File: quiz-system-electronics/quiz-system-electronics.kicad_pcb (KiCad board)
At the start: 2 copper layers, 25 parts, among them U1 74HC595, U2 74HC595, U3 74HC595, U4 ULN2803A, U5 ULN2803A

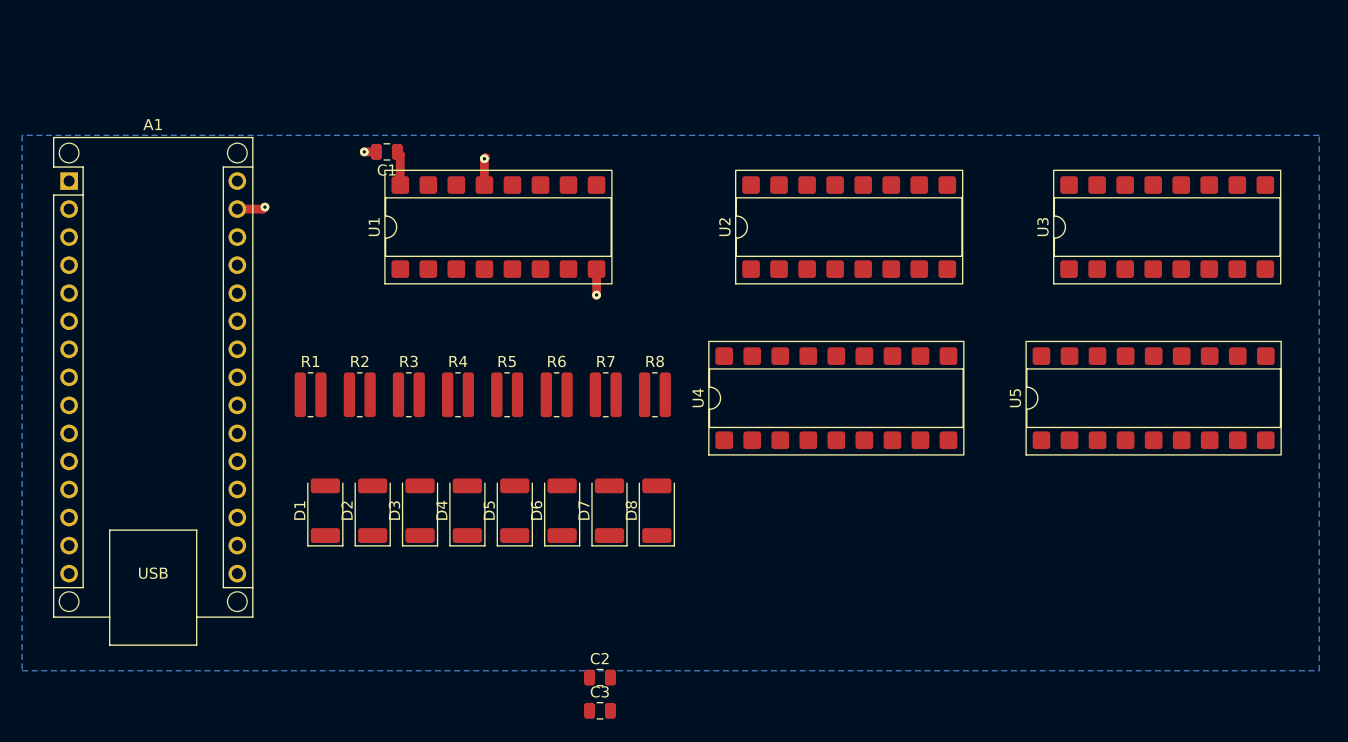
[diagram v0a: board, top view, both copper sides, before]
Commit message: Updated schematic and started to connect PCB
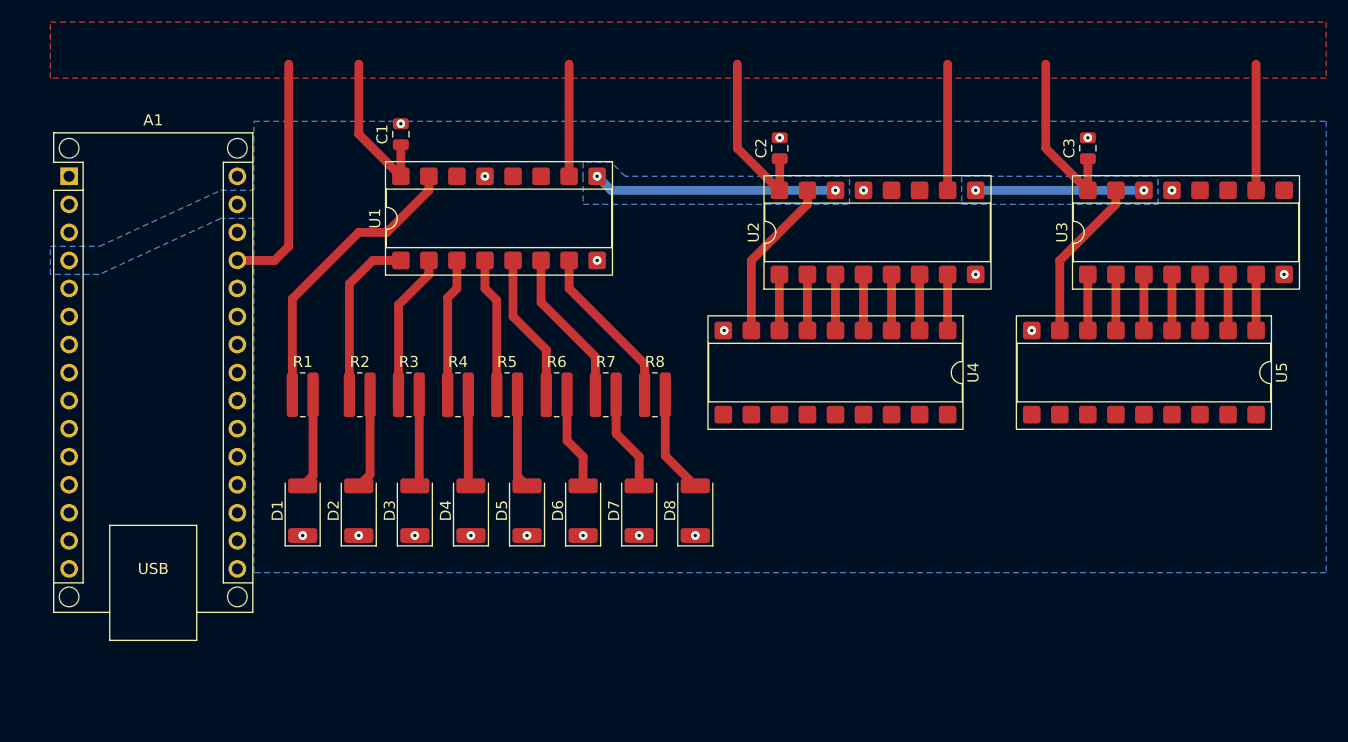
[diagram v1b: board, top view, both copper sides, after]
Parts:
- moved C3 67.5 mm to (129.5, 26.7), turned to 90 degrees
- moved C2 50.6 mm to (101.6, 26.7), turned to 90 degrees
- moved D8 3.48 mm to (94.0, 59.5)
- moved D7 2.69 mm to (88.9, 59.5)
- moved U2 2.61 mm to (110.5, 34.3)
- moved U5 2.48 mm to (134.6, 47.0), turned to -90 degrees
- moved U4 2.32 mm to (106.7, 47.0), turned to -90 degrees
- moved D1 2.05 mm to (58.4, 59.5)
- moved C1 2.04 mm to (67.3, 25.4), turned to 90 degrees
- moved D6 1.90 mm to (83.8, 59.5)
- moved U3 1.77 mm to (138.4, 34.3)
- moved D2 1.26 mm to (63.5, 59.5)
- moved D5 1.11 mm to (78.7, 59.5)
- moved U1 0.79 mm to (76.2, 33.0)
- moved R1 0.72 mm to (58.4, 49.0)
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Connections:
- U4 pad 1: Net-(U2-QA) -> Net-(U2-QH)
- U4 pad 2: Net-(U2-QB) -> Net-(U2-QG)
- U4 pad 3: Net-(U2-QC) -> Net-(U2-QF)
- U4 pad 4: Net-(U2-QD) -> Net-(U2-QE)
- U4 pad 5: Net-(U2-QE) -> Net-(U2-QD)
- U4 pad 6: Net-(U2-QF) -> Net-(U2-QC)
- U4 pad 7: Net-(U2-QG) -> Net-(U2-QB)
- U4 pad 8: Net-(U2-QH) -> Net-(U2-QA)
- U5 pad 1: Net-(U3-QA) -> Net-(U3-QH)
- U5 pad 2: Net-(U3-QB) -> Net-(U3-QG)
- U5 pad 3: Net-(U3-QC) -> Net-(U3-QF)
- U5 pad 4: Net-(U3-QD) -> Net-(U3-QE)
- U5 pad 5: Net-(U3-QE) -> Net-(U3-QD)
- U5 pad 6: Net-(U3-QF) -> Net-(U3-QC)
- U5 pad 7: Net-(U3-QG) -> Net-(U3-QB)
- U5 pad 8: Net-(U3-QH) -> Net-(U3-QA)
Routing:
- net +5V: track 3.11 -> 101.1 mm
- net Net-(U1-QA): track 0.00 -> 26.4 mm
- net QH' 1: track 0.00 -> 22.1 mm, vias 0 -> 2
- net Net-(U1-QB): track 0.00 -> 15.6 mm
- net QH' 2: track 0.00 -> 15.2 mm, vias 0 -> 2
- net Net-(U1-QH): track 0.00 -> 15.0 mm
- net Net-(U3-QA): track 0.00 -> 14.8 mm
- net Net-(U2-QA): track 0.00 -> 14.8 mm
- net Net-(U1-QG): track 0.00 -> 14.2 mm
- net Net-(U1-QF): track 0.00 -> 13.4 mm
- net Net-(U1-QC): track 0.00 -> 13.3 mm
- net Net-(U1-QE): track 0.00 -> 12.6 mm
- net Net-(U1-QD): track 0.00 -> 12.5 mm
- net Net-(D8-A): track 0.00 -> 9.38 mm
- net Net-(D7-A): track 0.00 -> 9.11 mm
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- added copper zone on F.Cu, net +5V
